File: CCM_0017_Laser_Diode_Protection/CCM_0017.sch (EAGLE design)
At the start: 6 parts, among them T1 FMMT4901, X1 22-23-2021, X2 22-23-2021

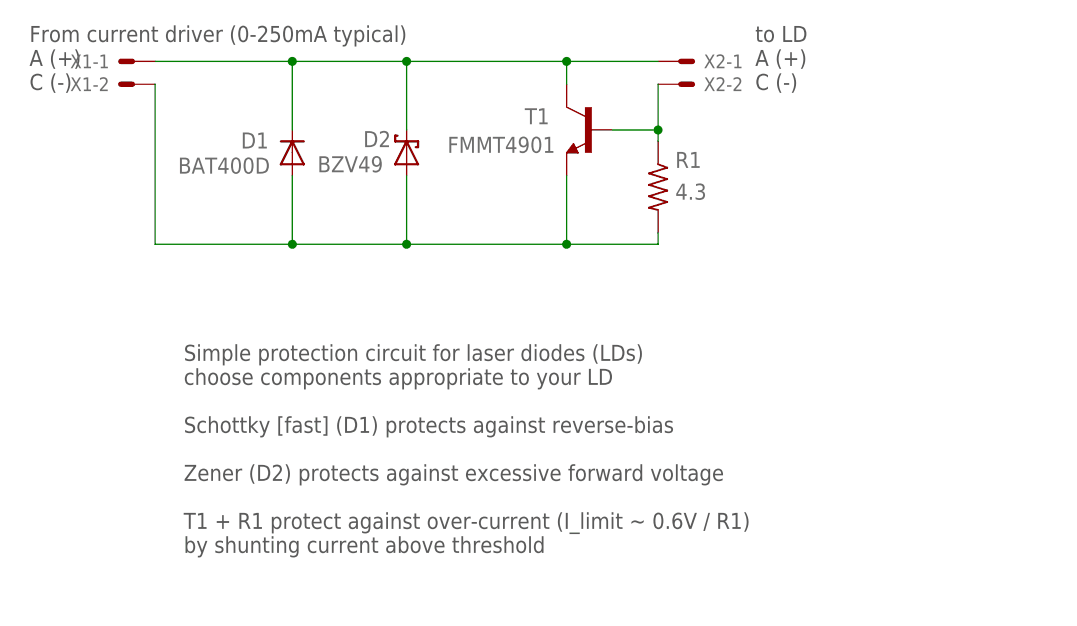
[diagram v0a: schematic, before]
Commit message: Shutter driver added.
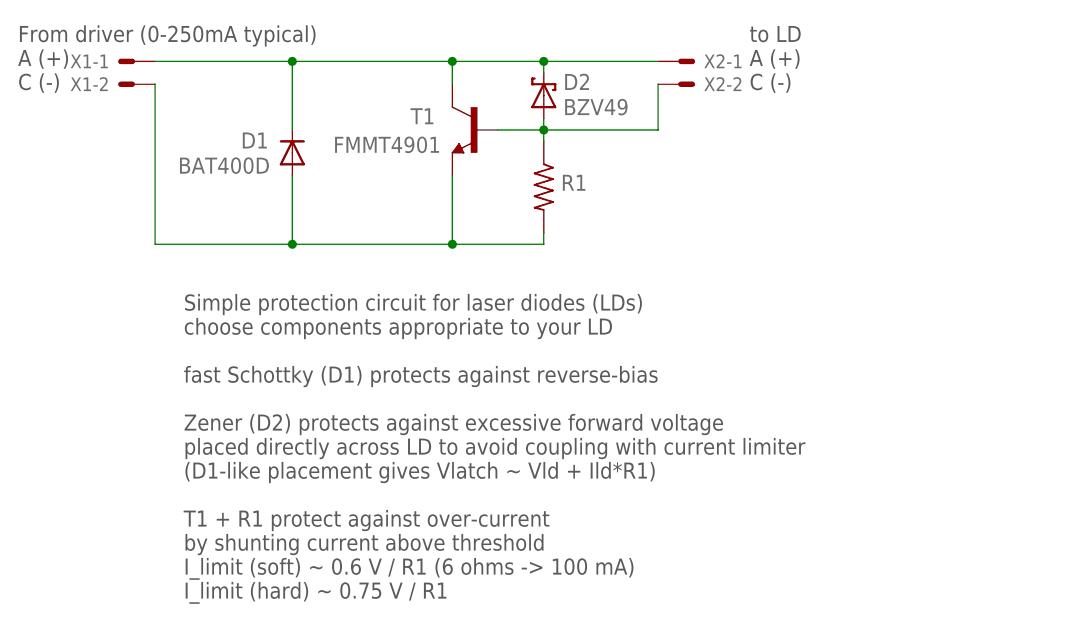
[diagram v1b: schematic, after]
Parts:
- R1: device noah:RESISTOR2512 -> noah:RESISTOR1210
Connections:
- net N$4: now also D2.A
- net N$5: no longer D2.A
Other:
- note added: "From driver (0-250mA typical) A (+) C (-)"
- note added: "Simple protection circuit for laser diodes (LDs) choose components appropriate to your LD fast Schottky (D1) protects against reverse-bias Zener (D2) protects against excessive forward voltage placed directly across LD to avoid coupling with current limiter (D1-like placement gives Vlatch ~ Vld + Ild*R1) T1 + R1 protect against over-current by shunting current above threshold I_limit (soft) ~ 0.6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"
- note removed: "From current driver (0-250mA typical) A (+) C (-)"
- note removed: "Simple protection circuit for laser diodes (LDs) choose components appropriate to your LD Schottky [fast] (D1) protects against reverse-bias Zener (D2) protects against excessive forward voltage T1 + R1 protect against over-current (I_limit ~ 0.6V / R1) by shunting current above threshold"
- moved on the sheet: D2, R1, T1
